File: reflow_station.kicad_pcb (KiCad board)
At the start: 6 copper layers, 180 x 110 mm, 267 parts, among them IC1 MP100LGN-Z, IC2 AMC23C10DWVR, J1 1731734, J10 USB_A, J11 USB_C_Receptacle_USB2.0_16P, J12 Conn_ARM_JTAG_SWD_10, J13 F52Q-1A7H1-11015, J2 1707027, J3 1707027, J4 1707027, J5 1707027, J6 DG301-5.0-02P-12-00A_H_, J7 DG301-5.0-02P-12-00A_H_, J8 DG301-5.0-02P-12-00A_H_, J9 DG301-5.0-02P-12-00A_H_, M1 Fan_CPU_4pin, M2 Fan_CPU_4pin, M3 Fan_CPU_4pin, M4 Fan_CPU_4pin, Q1 BTA16-600B, Q2 BTA16-600B, Q3 BTA16-600B, Q4 BTA16-600B, Q5 KSC1815YTA, SW2 SW_SPST, SW3 SW_SPST, SW4 SW_SPST, SW5 SW_DIP_x08, SW6 SW_Push, SW7 SW_SPDT, SW8 SW_SPDT, U1 TPS82130, U10 TPS2051BDBVR, U11 RCLAMP0504F.TCT, U12 RCLAMP0504F.TCT, U13 RCLAMP0504F.TCT, U14 STM32F469VIT6, U2 RAC20-12SK, U3 TPS82130, U4 MOC3052, U5 MOC3052, U6 MOC3052, U7 MOC3052, U8 ADS1118IDGS, U9 ADS1118IDGS, Y1 25MHz, Y2 32.768kHz

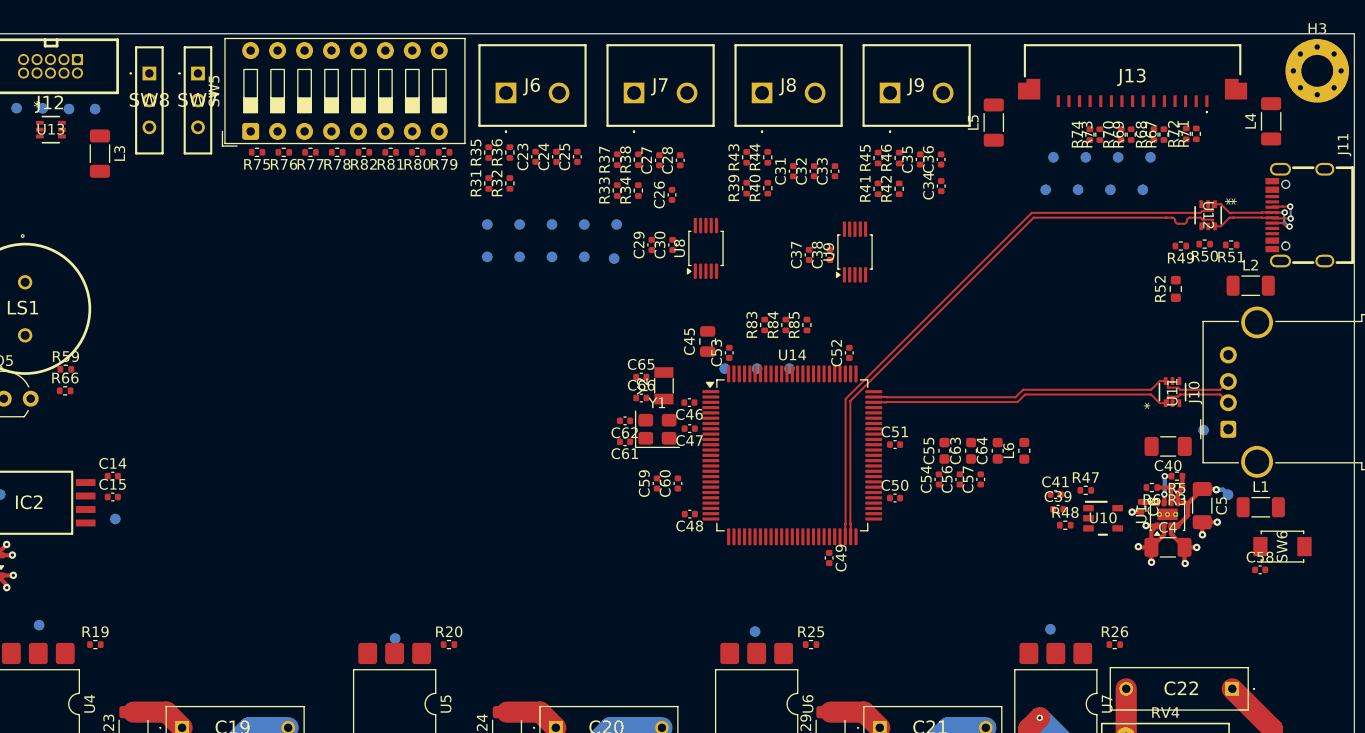
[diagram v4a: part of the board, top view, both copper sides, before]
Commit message: feat: calculate and sketch  differential pairs for MIPI DSI
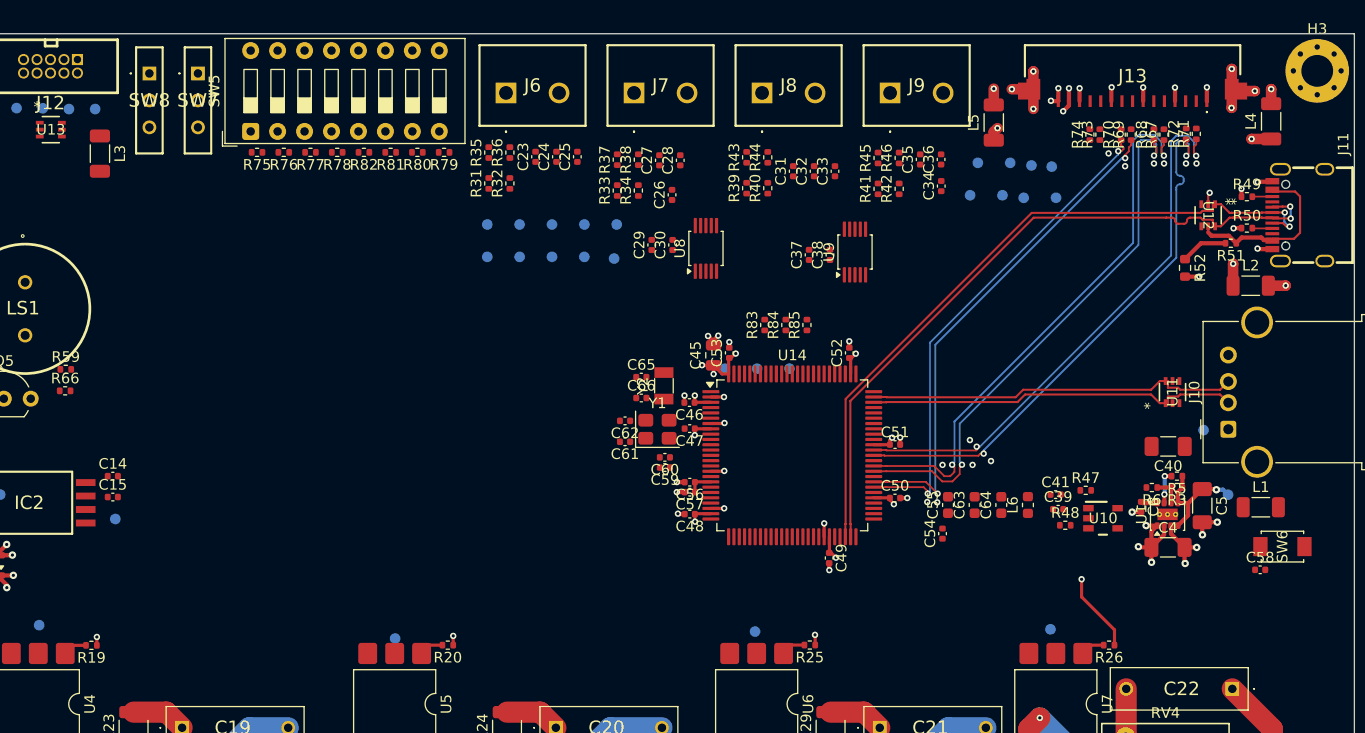
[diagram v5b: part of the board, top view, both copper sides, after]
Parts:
- moved C57 27.4 mm to (187.4, 83.2), turned to 180 degrees
- moved C56 25.5 mm to (187.4, 82.2), turned to 180 degrees
- moved TP26 9.35 mm to (221.5, 52.5)
- moved TP27 8.21 mm to (221.9, 55.4)
- moved TP28 8.21 mm to (219.6, 52.4)
- moved TP29 8.21 mm to (218.8, 55.4)
- moved R49 7.77 mm to (239.9, 55.3), turned to 0 degrees
- moved TP30 7.14 mm to (217.6, 52.1)
- moved TP31 7.14 mm to (216.8, 55.2)
- moved TP32 7.14 mm to (214.5, 52.1)
- moved TP33 7.14 mm to (213.8, 55.2)
- moved C54 5.12 mm to (211.2, 87.1)
- moved C55 5.12 mm to (211.7, 84.4)
- moved C63 5.12 mm to (214.2, 84.4)
- moved C64 5.12 mm to (216.7, 84.4)
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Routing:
- net /MCU/DSI1_CN: track 0.00 -> 52.8 mm, vias 0 -> 2
- net /User Interface/LCD/DSI1_DN1: track 0.00 -> 52.4 mm, vias 0 -> 2
- net /User Interface/LCD/DSI1_DP1: track 0.00 -> 52.3 mm, vias 0 -> 2
- net /MCU/DSI1_CP: track 0.00 -> 52.0 mm, vias 0 -> 2
- net /User Interface/LCD/DSI1_DN0: track 0.00 -> 47.7 mm, vias 0 -> 2
- net /User Interface/LCD/DSI1_DP0: track 0.00 -> 46.7 mm, vias 0 -> 2
- net +3V3: track 16.7 -> 52.7 mm, vias 5 -> 23
- net GND: track 42.4 -> 73.8 mm, vias 19 -> 60
- net Net-(J11-VBUS-PadA4): track 0.00 -> 16.4 mm
- net Earth: track 0.00 -> 16.1 mm, vias 0 -> 10
- net /Connectivity/USB_UART_VBUS_SENSE: track 0.00 -> 4.43 mm
- net +3.3VA: track 0.00 -> 2.46 mm
- net Net-(R26-Pad2): track 0.00 -> 2.30 mm
- net Net-(R25-Pad2): track 0.00 -> 2.29 mm
- net Net-(R20-Pad2): track 0.00 -> 2.29 mm
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
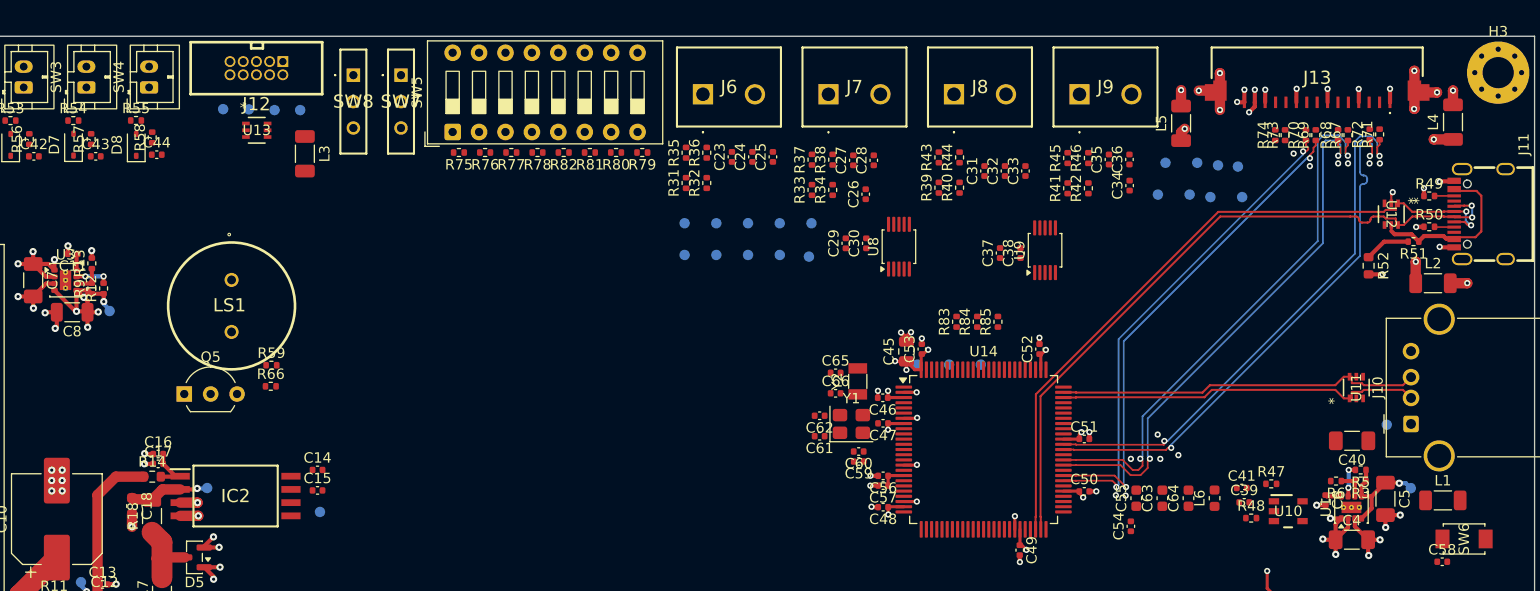
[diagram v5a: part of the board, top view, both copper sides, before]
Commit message: feat: tune differential pairs and reorder thermocouple sockets
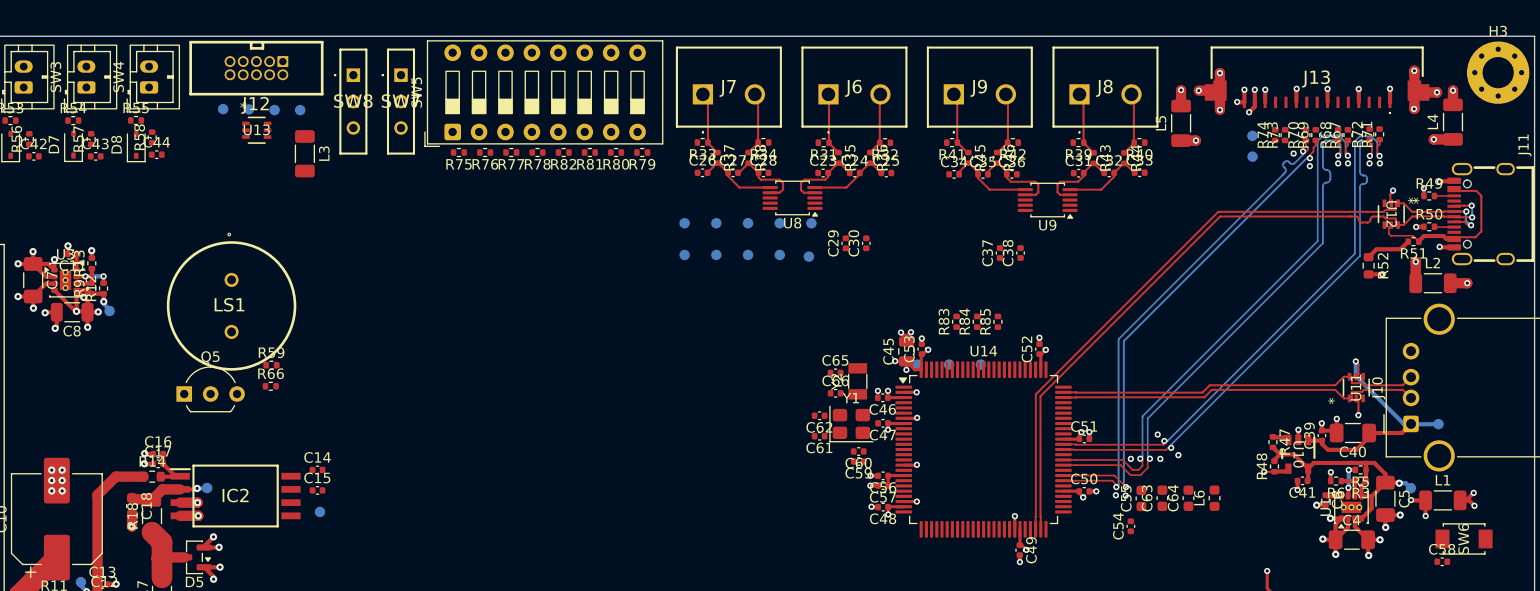
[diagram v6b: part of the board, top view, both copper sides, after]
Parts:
- removed TP26, TP27, TP28, TP29, TP30, TP32: TestPoint, reflow_station_library:TestPoint_Pad_D1.0mm
- moved R40 17.8 mm to (212.0, 50.2), turned to 180 degrees
- moved R32 17.6 mm to (187.6, 50.2), turned to 180 degrees
- moved C34 16.9 mm to (194.2, 53.2), turned to 0 degrees
- moved R44 15.8 mm to (210.6, 51.7), turned to -90 degrees
- moved C26 15.8 mm to (170.0, 53.1), turned to 0 degrees
- moved R36 15.7 mm to (186.1, 51.6), turned to -90 degrees
- moved R43 14.9 mm to (207.6, 51.7), turned to -90 degrees
- moved R35 14.7 mm to (183.1, 51.6), turned to -90 degrees
- moved R39 14.1 mm to (206.2, 50.2), turned to 180 degrees
- moved R31 13.8 mm to (181.7, 50.2), turned to 180 degrees
- moved C35 12.2 mm to (197.0, 53.2), turned to 0 degrees
- moved J9 12.1 mm to (194.2, 45.5)
- moved J7 12.1 mm to (170.0, 45.5)
- moved J8 12.1 mm to (206.2, 45.5)
- moved J6 12.1 mm to (182.1, 45.5)
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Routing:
- net Net-(J10-VBUS): track 0.00 -> 24.7 mm, vias 0 -> 1
- net +5V: track 10.7 -> 26.6 mm
- net GND: track 73.8 -> 83.2 mm, vias 60 -> 67
- net Net-(U9-AIN3): track 0.00 -> 8.69 mm
- net Net-(U9-AIN2): track 0.00 -> 8.33 mm
- net Net-(U8-AIN0): track 0.00 -> 8.19 mm
- net Net-(U9-AIN0): track 0.00 -> 7.93 mm
- net Net-(U9-AIN1): track 0.00 -> 7.84 mm
- net Net-(U8-AIN1): track 0.00 -> 7.82 mm
- net Net-(U8-AIN3): track 0.00 -> 7.74 mm
- net Net-(U8-AIN2): track 0.00 -> 7.58 mm
- net /Thermocouples/TC2+: track 0.00 -> 6.77 mm
- net /Thermocouples/TC4+: track 0.00 -> 6.71 mm
- net /Thermocouples/TC2-: track 0.00 -> 6.48 mm
- net /Thermocouples/TC4-: track 0.00 -> 6.38 mm
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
